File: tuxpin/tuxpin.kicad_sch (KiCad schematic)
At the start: 23 parts, among them Q1 BC817, Q2 BC817, Q3 BC817, Q4 BC817, Q5 BC817, Q6 BC817, U1 PST-540, U2 MAX16054AZT

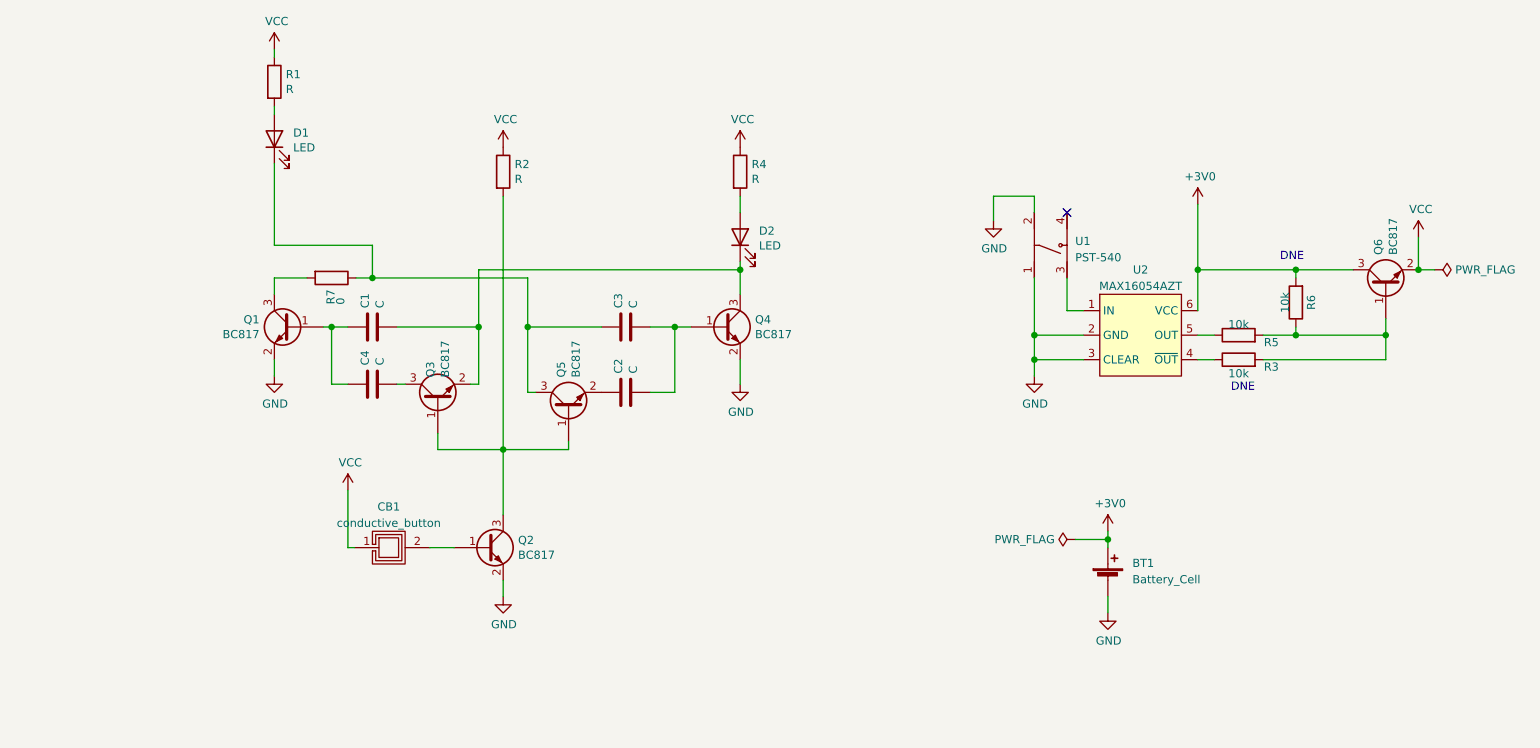
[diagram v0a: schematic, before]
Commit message: removed old gerbers, and created a updated final pcb
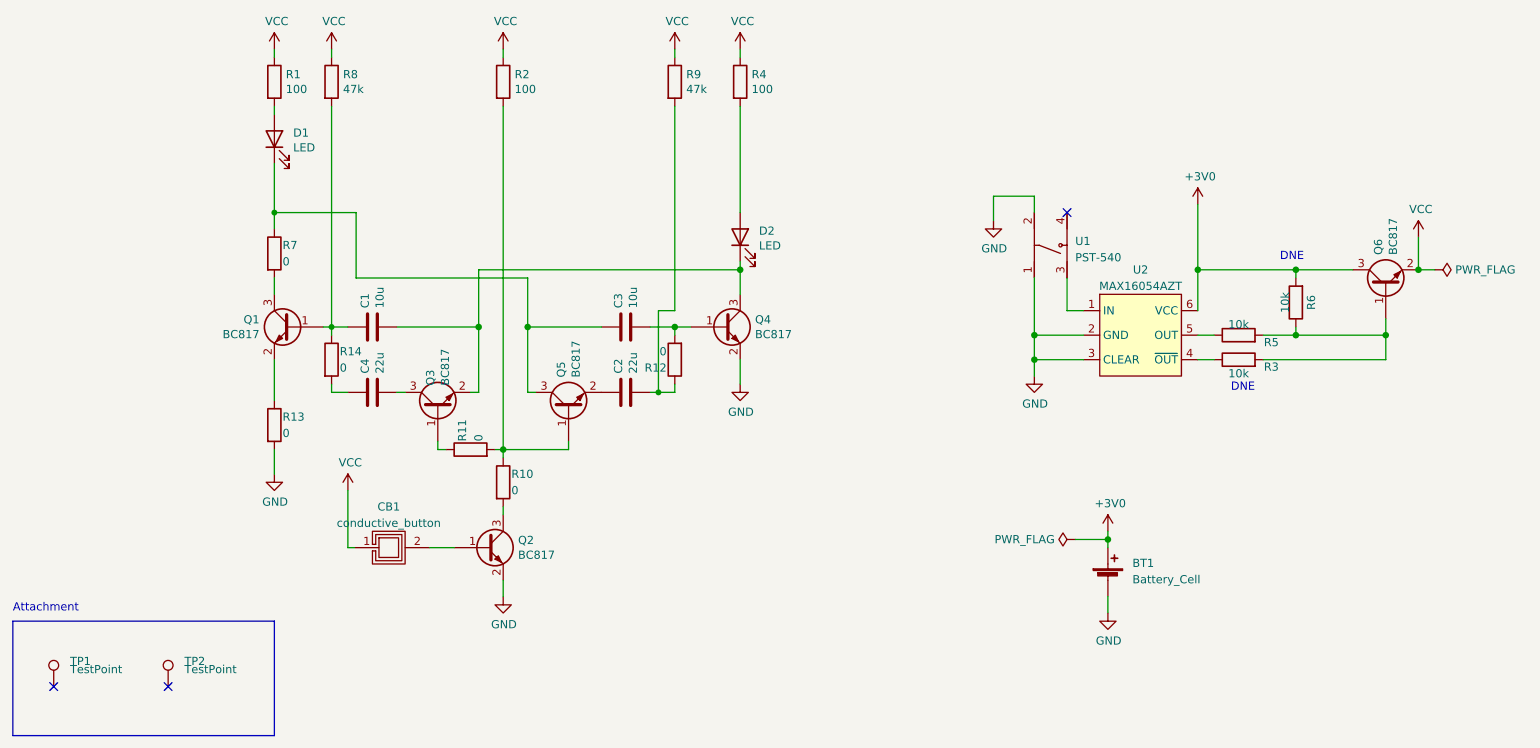
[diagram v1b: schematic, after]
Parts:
- added R10, R11, R12, R13, R14: 0, Resistor_SMD:R_0805_2012Metric_Pad1.20x1.40mm_HandSolder, symbol Device:R
- added R8, R9: 47k, Resistor_SMD:R_0603_1608Metric_Pad0.98x0.95mm_HandSolder, symbol Device:R
- added TP1, TP2: TestPoint, TestPoint:TestPoint_Pad_2.5x2.5mm, symbol Connector:TestPoint
- C1, C3: value C -> 10u; footprint Capacitor_SMD:C_0805_2012Metric_Pad1.18x1.45mm_HandSolder -> Capacitor_SMD:C_0603_1608Metric_Pad1.08x0.95mm_HandSolder
- C2, C4: value C -> 22u
- R1, R2, R4: value R -> 100; footprint Resistor_SMD:R_0805_2012Metric_Pad1.20x1.40mm_HandSolder -> Resistor_SMD:R_0603_1608Metric_Pad0.98x0.95mm_HandSolder
- R3, R5, R6: footprint Resistor_SMD:R_0805_2012Metric_Pad1.20x1.40mm_HandSolder -> Resistor_SMD:R_0603_1608Metric_Pad0.98x0.95mm_HandSolder
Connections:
- net GND: now also R13.2; no longer Q1.2 (E)
- net VCC: now also R8.1, R9.1
- net at Q5.1 (B), R2.2: now also R10.1, R11.2; no longer Q2.3 (C), Q3.1 (B)
- net at C1.2, Q1.1 (B): now also R14.1, R8.2; no longer C4.1
- net at C3.1, Q4.1 (B): now also R12.2; no longer C2.1
- new net: Q2.3 (C), R10.2
- new net: Q3.1 (B), R11.1
- new net: C2.1, R12.1, R9.2
- new net: C4.1, R14.2
- new net: Q1.2 (E), R13.1
- no-connect marks 1 -> 3
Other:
- note added: "Attachment"
- moved on the sheet: C4, Q3, R2, R4, R7

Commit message: changed bias point of the resistive button
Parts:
- R2: value 100 -> 100k
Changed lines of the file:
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@@
-(kicad_sch (version 20220104) (generator eeschema)
+(kicad_sch (version 20220126) (generator eeschema)
   (paper "A4")
   (junction (at 143.51 87.63) (diameter 0) (color 0 0 0 0)
@@
       (effects (font (size 1.27 1.27)) (justify left))
     )
-    (property "Value" "100" (id 1) (at 121.1581 40.5193 0)
+    (property "Value" "100k" (id 1) (at 121.1581 40.5193 0)
       (effects (font (size 1.27 1.27)) (justify left))
     )
@@
     )
     (path "/01df5f61-879b-4841-b017-2bce9ca1df1b"
-      (reference "R2") (unit 1) (value "100") (footprint "Resistor_SMD:R_0603_1608Metric_Pad0.98x0.95mm_HandSolder")
+      (reference "R2") (unit 1) (value "100k") (footprint "Resistor_SMD:R_0603_1608Metric_Pad0.98x0.95mm_HandSolder")
     )
     (path "/591e14ce-ba75-457a-a32d-167a4bde31a1"
